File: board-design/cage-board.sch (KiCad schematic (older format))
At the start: 57 parts, among them J1 Jack-DC, J10 73131-0240, J11 73131-0240, J12 73131-0240, J13 Conn_01x02, J14 Conn_01x02, J15 Conn_02x13_test_points, J16 TB002-500-03BE, J17 TB002-500-03BE, J18 TB002-500-03BE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

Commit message: auto push run at Fri Apr  9 12:23:24 EDT 2021
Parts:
- removed D1, D2: D_Small, Diode_SMD:D_SMA, symbol Device:D_Small
- added D1, D2: 1N4007, Diode_THT:D_DO-41_SOD81_P10.16mm_Horizontal, symbol Diode:1N4007
- R11, R13, R14, R16, R9: value 200 -> 1k; MFN RK73B2ATTD201J -> RK73B2ATTD102J; Supplier P/N 2019-RK73B2ATTD201JCT-ND -> 2019-RK73B2ATTD102JCT-ND
- R15: value 1k -> 10k; MFN RK73B2ATTD102J -> RK73B2ATTD103J; Supplier P/N 2019-RK73B2ATTD102JCT-ND -> 2019-RK73B2ATTD103JCT-ND
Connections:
- net +24V: now also D1.1 (K), D2.1 (K)
- net +5V: now also J16.1 (Pin_1), J17.1 (Pin_1), J18.1 (Pin_1); no longer J16.2 (Pin_2), J17.2 (Pin_2), J18.2 (Pin_2)
- net GND: now also J16.2 (Pin_2), J17.2 (Pin_2), J18.2 (Pin_2); no longer J16.3 (Pin_3), J17.3 (Pin_3), J18.3 (Pin_3)
- net P2.0: now also J16.3 (Pin_3); no longer J16.1 (Pin_1)
- net P2.1: now also J17.3 (Pin_3); no longer J17.1 (Pin_1)
- net P2.2: now also J18.3 (Pin_3); no longer J18.1 (Pin_1)
- net at J13.1 (Pin_1), Q1.1 (E): now also D1.2 (A)
- net at J14.1 (Pin_1), Q2.1 (E): now also D2.2 (A)
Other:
- moved on the sheet: J13, J14, J16, J17, J18, LED3, LED4, Q1, Q2, R1, R13, R14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

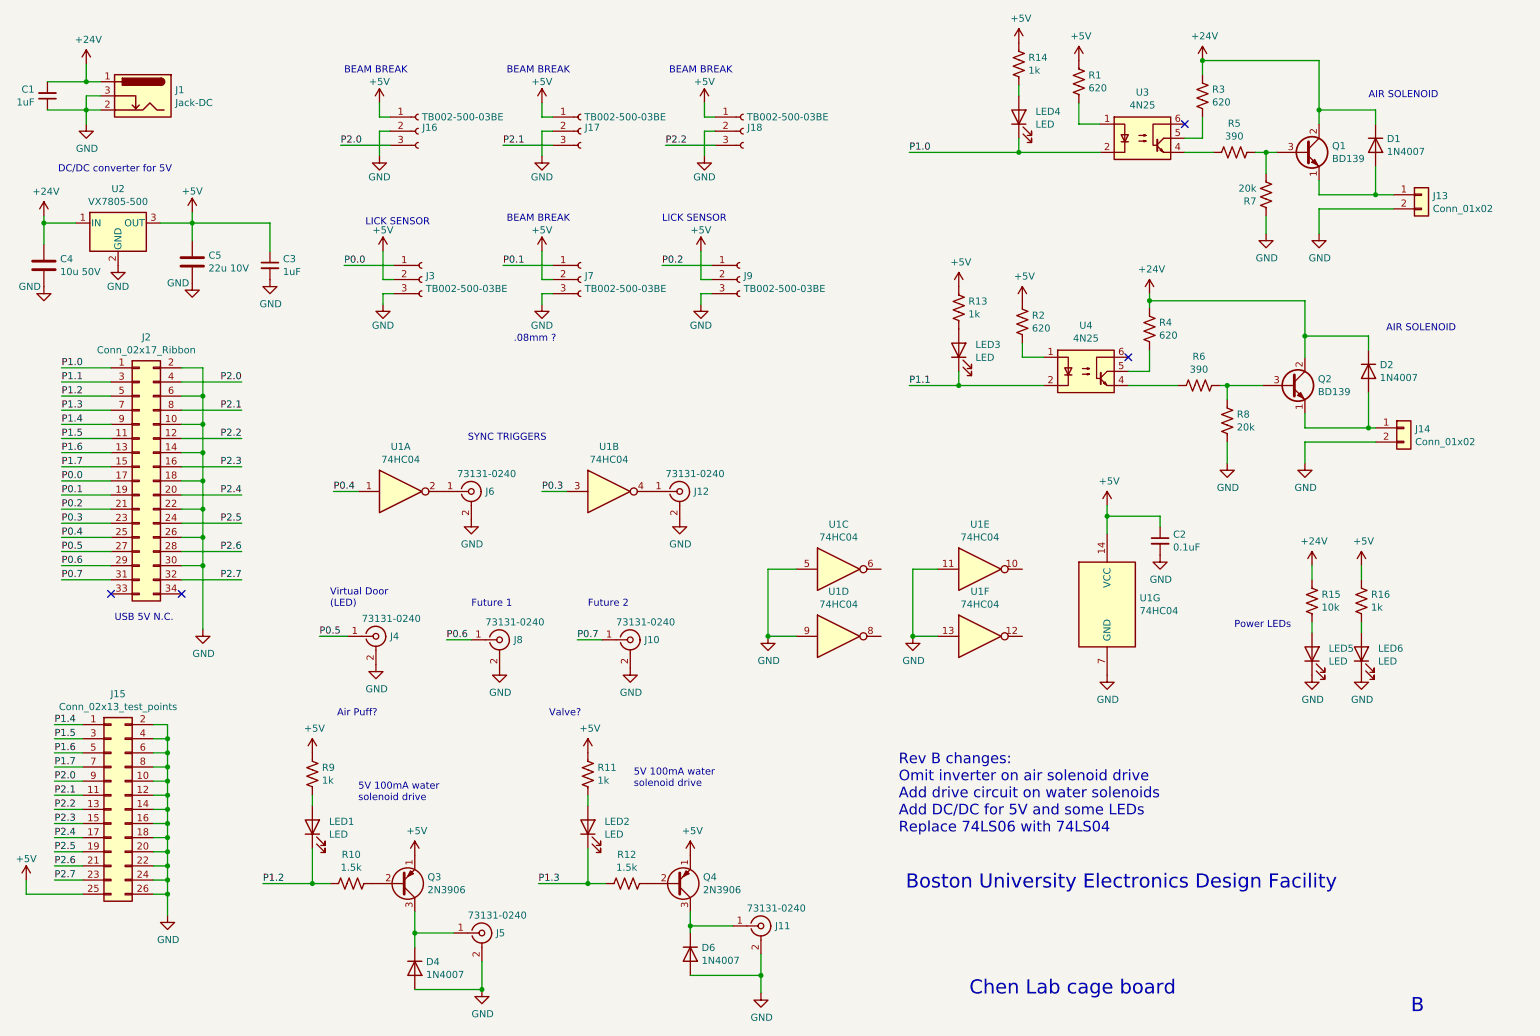
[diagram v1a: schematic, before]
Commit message: changin to right angle LEDs, fixing terminal blocks, fixing DC-DC footprint
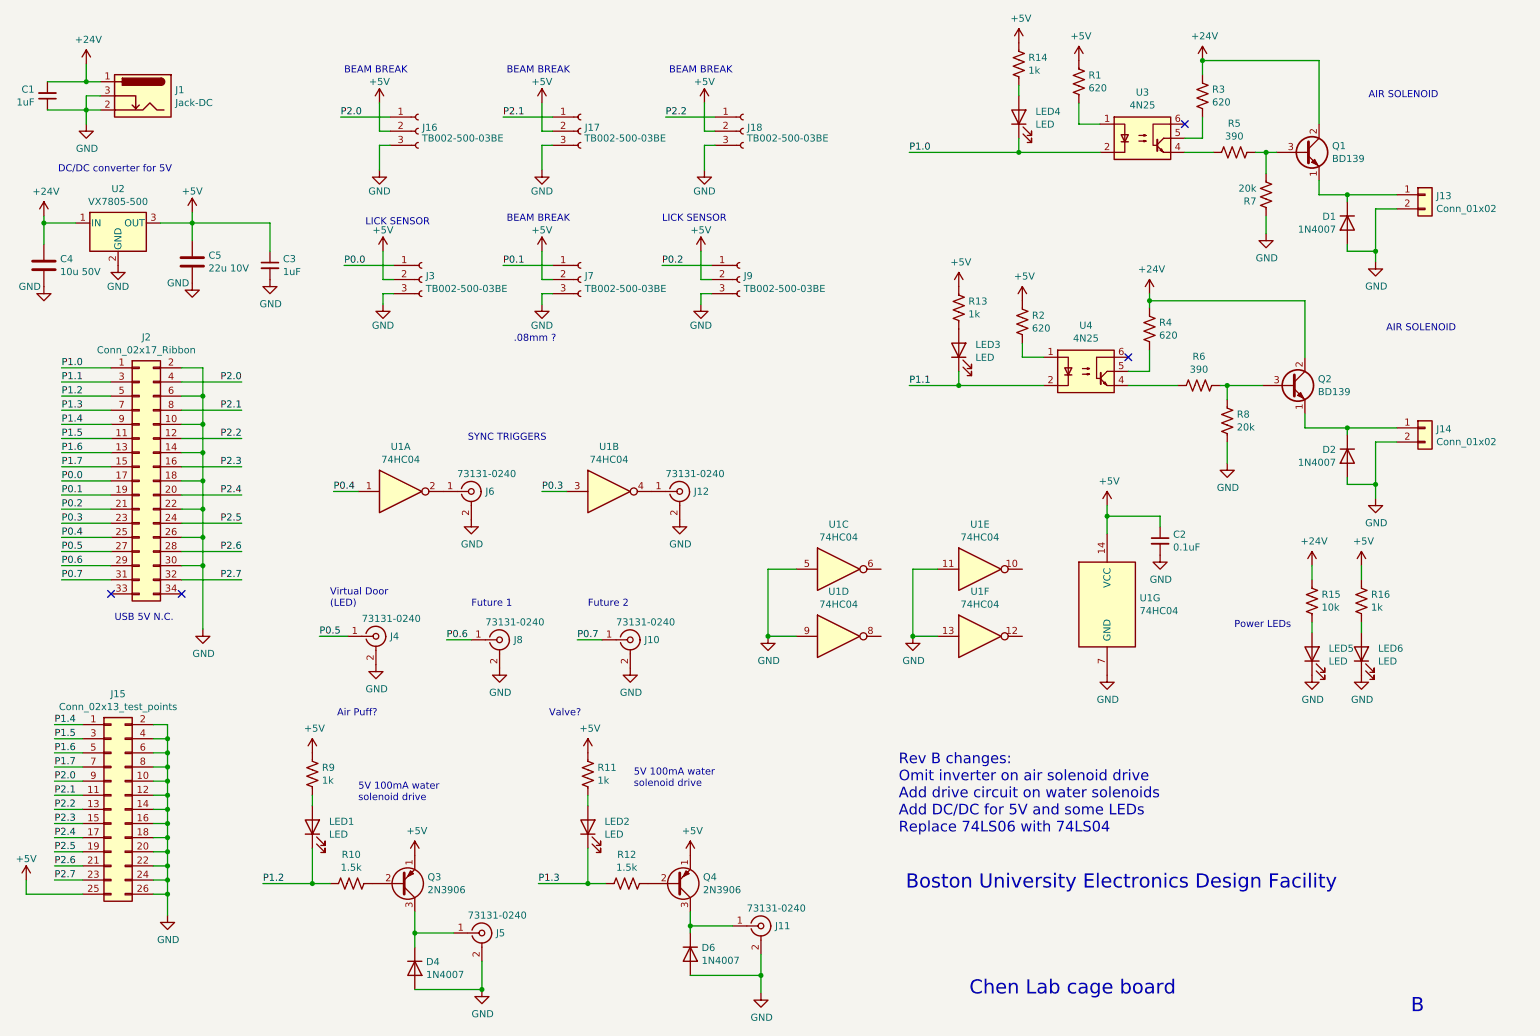
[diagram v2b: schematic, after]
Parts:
- LED1, LED2, LED3, LED4, LED5, LED6: footprint LED_THT:LED_D3.0mm -> LED_THT:LED_Rectangular_W5.0mm_H2.0mm; MFN LTW-420D7 -> WP1384AD/GD; Supplier P/N 160-1782-ND -> 754-1711-ND
- U2: footprint Package_TO_SOT_THT:TO-220-3_Vertical -> Package_SIP:SIP3_11.6x8.5mm
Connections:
- net +24V: no longer D1.1 (K), D2.1 (K)
- net +5V: now also J16.2 (Pin_2), J17.2 (Pin_2), J18.2 (Pin_2); no longer J16.1 (Pin_1), J17.1 (Pin_1), J18.1 (Pin_1)
- net GND: now also D1.2 (A), D2.2 (A), J16.3 (Pin_3), J17.3 (Pin_3), J18.3 (Pin_3); no longer J16.2 (Pin_2), J17.2 (Pin_2), J18.2 (Pin_2)
- net P2.0: now also J16.1 (Pin_1); no longer J16.3 (Pin_3)
- net P2.1: now also J17.1 (Pin_1); no longer J17.3 (Pin_3)
- net P2.2: now also J18.1 (Pin_1); no longer J18.3 (Pin_3)
- net at J13.1 (Pin_1), Q1.1 (E): now also D1.1 (K); no longer D1.2 (A)
- net at J14.1 (Pin_1), Q2.1 (E): now also D2.1 (K); no longer D2.2 (A)
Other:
- moved on the sheet: D1, D2, J13, J14

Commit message: all done except moving J13
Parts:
- removed C3: 1uF, Capacitor_SMD:C_0805_2012Metric_Pad1.15x1.40mm_HandSolder, symbol Device:C_Small
- removed C4: 10u 50V, Capacitor_SMD:C_1210_3225Metric_Pad1.33x2.70mm_HandSolder, symbol Device:C
- removed C5: 22u 10V, Capacitor_SMD:C_0805_2012Metric_Pad1.18x1.45mm_HandSolder, symbol Device:C
- removed LED1, LED2, LED3, LED4, LED5, LED6: LED, LED_THT:LED_Rectangular_W5.0mm_H2.0mm, symbol Device:LED
- removed R11, R13, R14, R16, R9: 1k, Resistor_SMD:R_0805_2012Metric_Pad1.20x1.40mm_HandSolder, symbol Device:R_US
- removed R15: 10k, Resistor_SMD:R_0805_2012Metric_Pad1.20x1.40mm_HandSolder, symbol Device:R_US
- removed U2: VX7805-500, Package_SIP:SIP3_11.6x8.5mm, symbol Regulator_Linear:uA7805
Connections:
- net +5V: now also J2.33 (Pin_33), J2.34 (Pin_34)
- no-connect marks 4 -> 2
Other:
- note added: "Rev C changes:\nDelete DC/DC for 5V and some LEDs\nMove J13 up to Rev A position"
- note removed: "DC/DC converter for 5V"
- note removed: "Power LEDs"
- note removed: "USB 5V N.C."

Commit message: Fix a couple of BOM issues
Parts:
- D1, D2, D4, D6: MFN XLUR34D -> 1N4007; Supplier P/N 1497-1491-ND -> 1N4007MSCT-ND
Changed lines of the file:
@@
 F 2 "Diode_THT:D_DO-41_SOD81_P10.16mm_Horizontal" H 3550 7150 50  0001 C CNN
 F 3 "http://www.vishay.com/docs/88503/1n4001.pdf" H 3550 7325 50  0001 C CNN
-F 4 "XLUR34D" H 3550 7325 50  0001 C CNN "MFN"
+F 4 "1N4007" H 3550 7325 50  0001 C CNN "MFN"
 F 5 "Digi-Key" H 3550 7325 50  0001 C CNN "Supplier"
-F 6 "1497-1491-ND" V 3550 7325 50  0001 C CNN "Supplier P/N"
+F 6 "1N4007MSCT-ND" V 3550 7325 50  0001 C CNN "Supplier P/N"
 F 7 "0.31" H 3550 7325 50  0001 C CNN "Item Cost"
 	1    3550 7325
@@
 F 2 "Diode_THT:D_DO-41_SOD81_P10.16mm_Horizontal" H 5500 7050 50  0001 C CNN
 F 3 "http://www.vishay.com/docs/88503/1n4001.pdf" H 5500 7225 50  0001 C CNN
-F 4 "1497-1491-ND" H 5500 7225 50  0001 C CNN "Supplier P/N"
-F 5 "XLUR34D" H 5500 7225 50  0001 C CNN "MFN"
+F 4 "1N4007MSCT-ND" H 5500 7225 50  0001 C CNN "Supplier P/N"
+F 5 "1N4007" H 5500 7225 50  0001 C CNN "MFN"
 F 6 "Digi-Key" H 5500 7225 50  0001 C CNN "Supplier"
 F 7 "0.31" H 5500 7225 50  0001 C CNN "Item Cost"
@@
 F 2 "Diode_THT:D_DO-41_SOD81_P10.16mm_Horizontal" H 10150 3525 50  0001 C CNN
 F 3 "http://www.vishay.com/docs/88503/1n4001.pdf" H 10150 3700 50  0001 C CNN
-F 4 "XLUR34D" H 10150 3700 50  0001 C CNN "MFN"
+F 4 "1N4007" H 10150 3700 50  0001 C CNN "MFN"
 F 5 "Digi-Key" H 10150 3700 50  0001 C CNN "Supplier"
-F 6 "1497-1491-ND" V 10150 3700 50  0001 C CNN "Supplier P/N"
+F 6 "1N4007MSCT-ND" V 10150 3700 50  0001 C CNN "Supplier P/N"
 F 7 "0.31" H 10150 3700 50  0001 C CNN "Item Cost"
 	1    10150 3700
@@
 F 2 "Diode_THT:D_DO-41_SOD81_P10.16mm_Horizontal" H 10150 1875 50  0001 C CNN
 F 3 "http://www.vishay.com/docs/88503/1n4001.pdf" H 10150 2050 50  0001 C CNN
-F 4 "1497-1491-ND" H 10150 2050 50  0001 C CNN "Supplier P/N"
-F 5 "XLUR34D" H 10150 2050 50  0001 C CNN "MFN"
+F 4 "1N4007MSCT-ND" H 10150 2050 50  0001 C CNN "Supplier P/N"
+F 5 "1N4007" H 10150 2050 50  0001 C CNN "MFN"
 F 6 "Digi-Key" H 10150 2050 50  0001 C CNN "Supplier"
 F 7 "0.31" H 10150 2050 50  0001 C CNN "Item Cost"
@@
 	7050 1550 8400 1550
 $Comp
-L power:+5V #PWR?
+L power:+5V #PWR0130
 U 1 1 60BB4519
 P 1050 4975
-F 0 "#PWR?" H 1050 4825 50  0001 C CNN
+F 0 "#PWR0130" H 1050 4825 50  0001 C CNN
 F 1 "+5V" H 1050 5125 50  0000 C CNN
 F 2 "" H 1050 4975 50  0001 C CNN
